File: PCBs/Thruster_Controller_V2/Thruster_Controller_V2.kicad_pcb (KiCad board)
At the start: 4 copper layers, 36 x 37.5 mm, 110 parts, among them J1 PHASE_A, J2 PHASE_B, J3 PHASE_C, J4 Conn_01x01, J5 Pogo Conn, J6 Conn_01x01, J7 Conn_01x01, J8 Conn_01x01, Q1 SIZF906DT, Q2 SIZF906DT, Q3 SIZF906DT, U1 DRV8305, U2 RTQ2569-50GQW, U3 MCP2515, U4 TPS62172DSGR, U5 TMS320F28027F, U8 MCP2562, Y1 20MHz

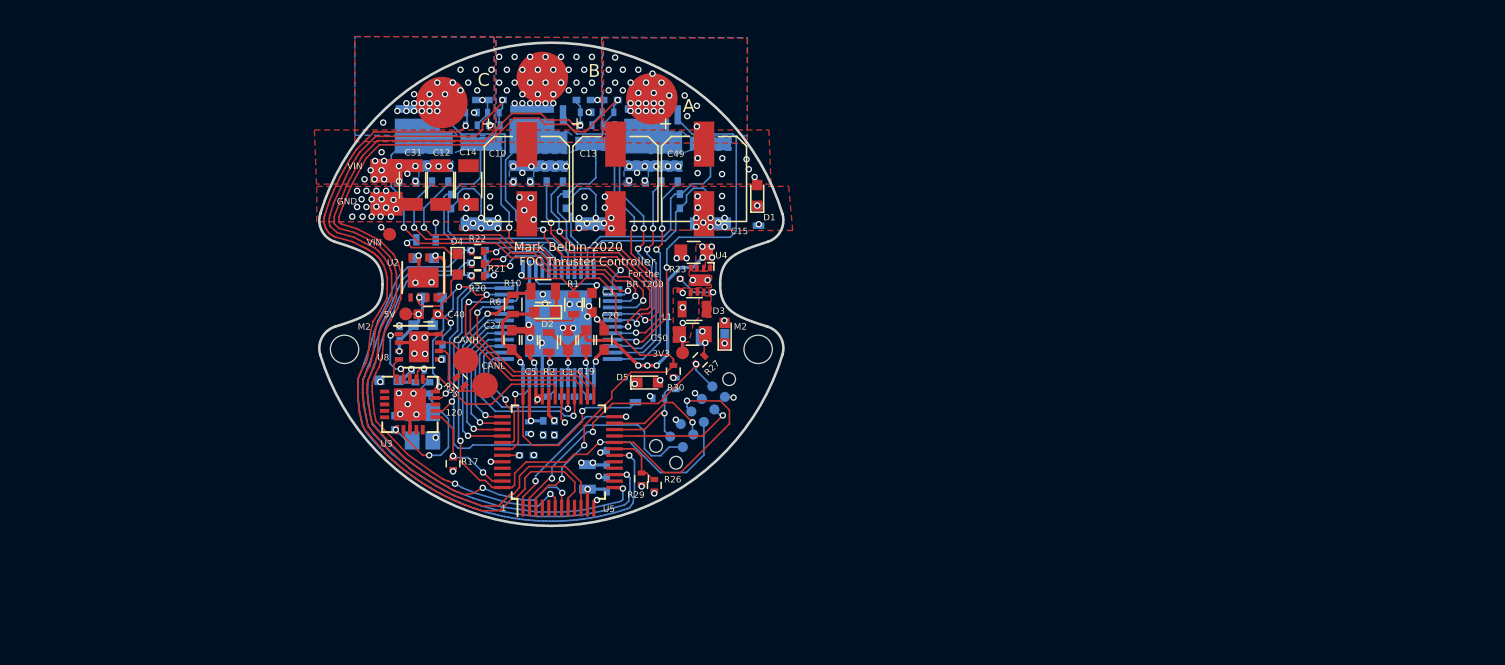
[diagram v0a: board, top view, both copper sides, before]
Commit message: Started Layout
- Imported new netlist
- Ripped up old tracks
- Added new outline
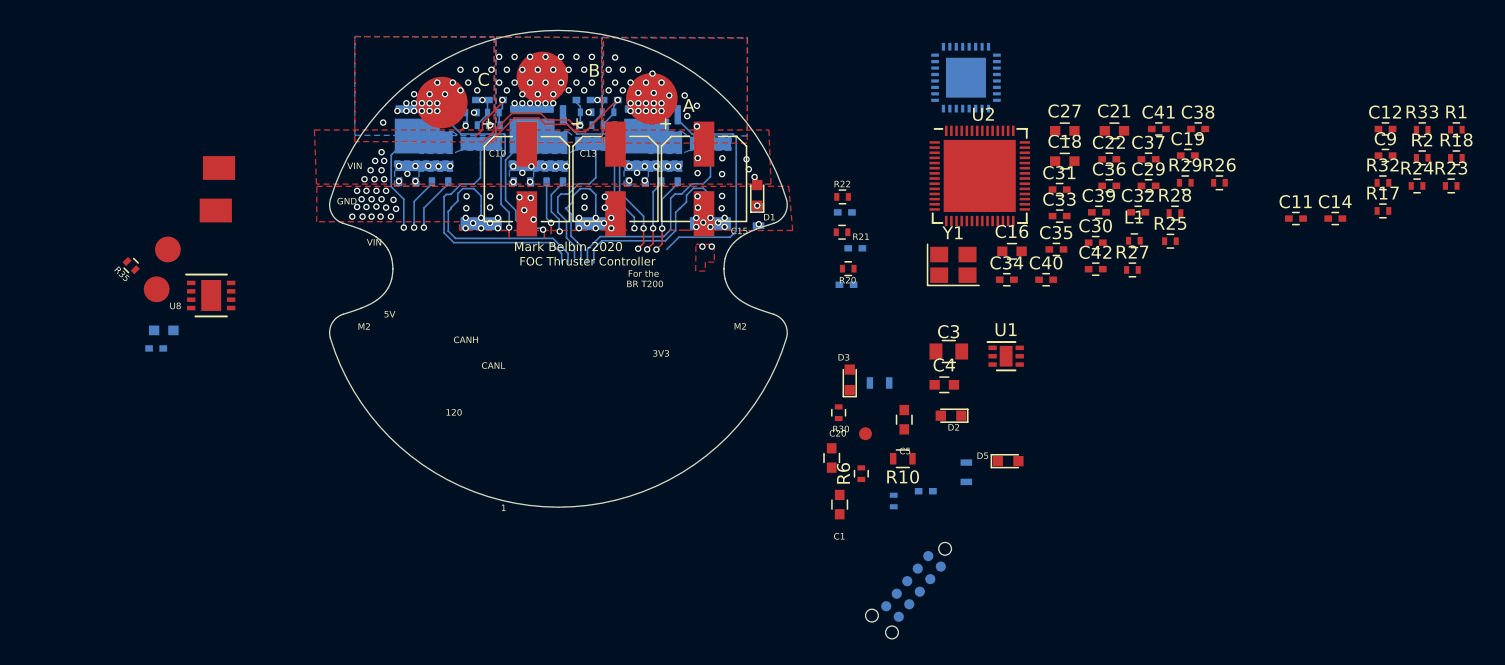
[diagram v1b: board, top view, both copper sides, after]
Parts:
- removed C49: 10uF, Capacitors_SMD:C_0805
- removed C50: 22uF, Capacitors_SMD:C_0805
- removed D4: RED, LEDs:LED_0603
- removed H1, H2: MountingHole, Thruster_Controller:MountingHole_M2
- removed L2: FB, Inductors_SMD:L_0805
- removed TP2, TP3: TestPoint, Thruster_Controller:TestPoint_Pad_D1.0mm
- removed U4: TPS62172DSGR, Thruster_Controller:8-Pin_WSON
- removed U5: TMS320F28027F, Housings_QFP:LQFP-48_7x7mm_Pitch0.5mm
- added C11: 0.01uF, Capacitors_SMD:C_0402, F.Cu at (157.2, 94.3)
- added C32: 2.2uF, Capacitors_SMD:C_0402, F.Cu at (145.0, 93.9)
- added C33: 0.1uF, Capacitors_SMD:C_0402, F.Cu at (138.9, 94.2)
- added R32: 2.49k, Resistors_SMD:R_0402, F.Cu at (164.0, 91.6)
- added R33: 56, Resistors_SMD:R_0402, F.Cu at (167.0, 87.5)
- C10, C13, C15: value 22uF -> 220uF
- C12, C14: value 22uF -> 0.01uF; footprint Capacitors_SMD:C_1206 -> Capacitors_SMD:C_0402
- C16, C18: value 1000pF -> 10uF; footprint Capacitors_SMD:C_0402 -> Capacitors_SMD:C_0603; moved to F.Cu
- C19: footprint Capacitors_SMD:C_0603 -> Capacitors_SMD:C_0402
- C21: value 15pF -> 10uF; footprint Capacitors_SMD:C_0402 -> Capacitors_SMD:C_0603; moved to F.Cu
- C22: value 15pF -> 2.2uF; moved to F.Cu
- C27: value 1uF -> 10uF
- C29: value 1uF -> 2.2uF; footprint Capacitors_SMD:C_0603 -> Capacitors_SMD:C_0402; moved to F.Cu
- C3: footprint Capacitors_SMD:C_0603 -> Capacitors_SMD:C_0805
- C30: value 0.1uF -> 2.2uF; moved to F.Cu
- C31: value 22uF -> 0.1uF; footprint Capacitors_SMD:C_1206 -> Capacitors_SMD:C_0402
- C34, C38: value 2.2uF -> 0.1uF; moved to F.Cu
- C35: value 2.2uF -> 10nF; moved to F.Cu
- C36, C37: value 2.2uF -> 9pF; moved to F.Cu
- C39, C41: value 1uF -> 0.1uF; footprint Capacitors_SMD:C_0603 -> Capacitors_SMD:C_0402; moved to F.Cu
- C4: value 0.047uF -> 1uF; footprint Capacitors_SMD:C_0402 -> Capacitors_SMD:C_0603; moved to F.Cu
- C40: value 1uF -> 0.1uF; footprint Capacitors_SMD:C_0603 -> Capacitors_SMD:C_0402
- C42: moved to F.Cu
- C9: value 1000pF -> 0.1uF; moved to F.Cu
- L1: value 2.2uH -> 220 Ohm; footprint Inductors_SMD:L_0805 -> Inductors_SMD:L_0402
- L3: value FB -> 60 Ohm
- R1: value 10k -> 2.2k; footprint Resistors_SMD:R_0603 -> Resistors_SMD:R_0402
- R10, R19: footprint Resistors_SMD:R_0805 -> Resistors_SMD:R_0603
- R17: value 10k -> 27.4k
- R18: value 10k -> 27.4k; moved to F.Cu
- R2: value 100 -> 27.4k; footprint Resistors_SMD:R_0603 -> Resistors_SMD:R_0402
- R23: value 100k -> 2.49k; footprint Resistors_SMD:R_0402_NoSilk -> Resistors_SMD:R_0402
- R24: value 680 -> 2.49k; footprint Resistors_SMD:R_0603 -> Resistors_SMD:R_0402; moved to F.Cu
- R25: value 820 -> 10k; moved to F.Cu
- R26: value 820 -> 10k
- R28: value 2.2k -> 10k; moved to F.Cu
- R29: value 2.2k -> 10k
- R6: footprint Resistors_SMD:R_0603 -> Resistors_SMD:R_0402
- U1: value DRV8305 -> NCP718AMT330; footprint Thruster_Controller:DRV8305 -> Housings_DFN_QFN:DFN-6-1EP_2x2mm_Pitch0.65mm; moved to F.Cu
- U2: value RTQ2569-50GQW -> TMS320F280041C; footprint Housings_DFN_QFN:DFN-8-1EP_3x3mm_Pitch0.65mm -> Housings_DFN_QFN:QFN-56-1EP_7x7mm_Pitch0.4mm
- U3: value MCP2515 -> DRV8320S; footprint Housings_DFN_QFN:QFN-20-1EP_4x4mm_Pitch0.5mm -> Housings_DFN_QFN:WQFN-32-1EP_5x5mm_Pitch0.5mm; moved to B.Cu
- Y1: value 20MHz -> 20 MHz; footprint Crystals:Crystal_SMD_SeikoEpson_TSX3225-4pin_3.2x2.5mm -> Crystals:Crystal_SMD_SeikoEpson_FA238-4pin_3.2x2.5mm; moved to F.Cu
- moved R18 82.2 mm to (169.7, 89.6)
- moved R24 77.0 mm to (166.6, 91.8)
- moved R17 74.8 mm to (164.0, 93.8), turned to 0 degrees
- moved C12 73.5 mm to (164.2, 87.4), turned to 0 degrees
- moved R1 69.8 mm to (169.7, 87.5), turned to 0 degrees
- moved R2 69.3 mm to (167.0, 89.6), turned to 0 degrees
- moved C14 67.3 mm to (160.3, 94.3), turned to 0 degrees
- moved R23 60.3 mm to (169.3, 91.8), turned to 0 degrees
- moved C21 60.3 mm to (143.1, 87.5), turned to 0 degrees
- moved C41 57.9 mm to (146.6, 87.4)
- moved C29 57.3 mm to (145.8, 91.8)
- moved C22 56.3 mm to (142.7, 89.7), turned to 0 degrees
- moved C38 55.1 mm to (149.6, 87.4), turned to 0 degrees
- moved C9 54.9 mm to (164.2, 89.5), turned to 0 degrees
- moved C30 54.5 mm to (141.7, 96.2), turned to 0 degrees
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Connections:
- net /TI_MCU/ADCINB7 renamed Net-(C26-Pad1)
- C12 pad 2: GND -> /Powertrain/SL_B
- C14 pad 2: GND -> /Powertrain/SL_C
- C16 pad 1: /Powertrain/SN2 -> +3V3
- C16 pad 2: /Powertrain/SP2 -> GND
- C17 pad 1: /TI_MCU/ADCINA0 -> /Powertrain/VSEN_C
- C18 pad 1: /Powertrain/SN3 -> +3V3
- C18 pad 2: /Powertrain/SP3 -> GND
- C19 pad 1: +BATT -> +3V3
- C19 pad 2: Net-(C19-Pad2) -> GND
- C21 pad 1: Net-(C21-Pad1) -> +3V3
- C24 pad 1: /TI_MCU/ADCINB1 -> Net-(C24-Pad1)
- C24 pad 2: GND -> /Powertrain/PGA_GND
- C25 pad 1: /TI_MCU/ADCINB3 -> Net-(C25-Pad1)
- C25 pad 2: GND -> /Powertrain/PGA_GND
- C26 pad 2: GND -> /Powertrain/PGA_GND
- C27 pad 1: +3V3 -> +3.3VA
- C29 pad 1: +5V -> Net-(C22-Pad1)
- C3 pad 1: Net-(C3-Pad1) -> +BATT
- C30 pad 1: +5V -> Net-(C30-Pad1)
- C31 pad 1: +BATT -> +3V3
- C34 pad 1: Net-(C34-Pad1) -> +3.3VA
- C35 pad 1: +3V3 -> /TI_MCU/~RESET~
- C36 pad 1: Net-(C36-Pad1) -> /TI_MCU/X1
- C37 pad 1: Net-(C37-Pad1) -> /TI_MCU/X2
- C38 pad 1: Net-(C38-Pad1) -> +3V3
- C39 pad 1: +BATT -> +3.3VA
- C4 pad 1: Net-(C4-Pad1) -> +3V3
- C4 pad 2: Net-(C4-Pad2) -> GND
- C40 pad 1: +5V -> +3.3VA
- C41 pad 1: +5V -> +3V3
- C42 pad 1: +3V3 -> +3.3VA
- C5 pad 1: Net-(C5-Pad1) -> +BATT
- C5 pad 2: GND -> Net-(C5-Pad2)
- C6 pad 1: /TI_MCU/ADCINA3 -> /Powertrain/VSEN_B
- C7 pad 1: /TI_MCU/ADCINA1 -> /Powertrain/VSEN_C
- C8 pad 1: /TI_MCU/ADCINA7 -> /Powertrain/VSEN_A
- C9 pad 1: /Powertrain/SN1 -> +BATT
- C9 pad 2: /Powertrain/SP1 -> GND
- J5 pad 3: /GPIO28 -> /SCI_TX
- J5 pad 5: /GPIO29 -> /SCI_RX
- L1 pad 1: Net-(L1-Pad1) -> +3V3
- L1 pad 2: +3V3 -> +3.3VA
- L3 pad 2: Net-(C37-Pad1) -> Net-(C22-Pad1)
- NT1 pad 1: /Powertrain/SP2 -> /Powertrain/SNA
- NT2 pad 1: /Powertrain/SP3 -> /Powertrain/SNA
- NT3 pad 1: /Powertrain/SP1 -> /Powertrain/SNA
- NT4 pad 1: /Powertrain/SN2 -> /Powertrain/SPB
- NT5 pad 1: /Powertrain/SN3 -> /Powertrain/SPC
- NT6 pad 1: /Powertrain/SN1 -> /Powertrain/SPA
- R1 pad 2: /Powertrain/PWRGD -> /Powertrain/SPI_MISO
- R10 pad 2: /GPIO28 -> /Powertrain/nFAULT
- R12 pad 1: /TI_MCU/ADCINA3 -> /Powertrain/VSEN_B
- R13 pad 1: /TI_MCU/ADCINA1 -> /Powertrain/VSEN_C
- R14 pad 1: /TI_MCU/ADCINA7 -> /Powertrain/VSEN_A
- R15 pad 2: /TI_MCU/ADCINA0 -> /Powertrain/VSEN_C
- R16 pad 1: /TI_MCU/ADCINA0 -> /Powertrain/VSEN_C
- R17 pad 1: +3V3 -> /Powertrain/ISEN_B
- R17 pad 2: /TI_MCU/CAN_INT -> /Powertrain/DAC
- R18 pad 1: +3V3 -> /Powertrain/ISEN_C
- R18 pad 2: Net-(R18-Pad2) -> /Powertrain/DAC
- R2 pad 1: +BATT -> /Powertrain/ISEN_A
- R2 pad 2: Net-(R2-Pad2) -> /Powertrain/DAC
- R20 pad 1: /Powertrain/ISEN_A_DRV -> /Powertrain/SPA
- R20 pad 2: /TI_MCU/ADCINB1 -> Net-(C24-Pad1)
- R21 pad 1: /Powertrain/ISEN_B_DRV -> /Powertrain/SPB
- R21 pad 2: /TI_MCU/ADCINB3 -> Net-(C25-Pad1)
- R22 pad 1: /Powertrain/ISEN_C_DRV -> /Powertrain/SPC
- R23 pad 1: +3V3 -> Net-(C24-Pad1)
- R23 pad 2: Net-(R23-Pad2) -> /Powertrain/ISEN_A
- R24 pad 1: Net-(D4-Pad1) -> Net-(C25-Pad1)
- R24 pad 2: GND -> /Powertrain/ISEN_B
- R25 pad 2: /TDO -> /TDI
- R26 pad 2: /TI_MCU/GPIO34 -> /TDO
- R27 pad 1: /TRST -> +3V3
- R27 pad 2: GND -> /TMS
- R28 pad 1: /TDO -> +3V3
- R28 pad 2: GND -> /TI_MCU/GPIO32
- R29 pad 1: /TI_MCU/GPIO34 -> +3V3
- R29 pad 2: GND -> /TI_MCU/GPIO24
- R3 pad 2: /TI_MCU/ADCINA3 -> /Powertrain/VSEN_B
- R30 pad 2: /Powertrain/PWRGD -> /TI_MCU/~RESET~
- R31 pad 2: /TI_MCU/GPIO33 -> /TI_MCU/GPIO6
- R4 pad 2: /TI_MCU/ADCINA1 -> /Powertrain/VSEN_C
- R5 pad 2: /TI_MCU/ADCINA7 -> /Powertrain/VSEN_A
- R6 pad 2: /GPIO28 -> /Powertrain/nFAULT
- U1 pad 1: /Powertrain/EN_GATE -> +3V3
- U1 pad 2: /TI_MCU/EPWM1A -> GND
- U1 pad 3: /TI_MCU/EPWM1B -> GND
- U1 pad 4: /TI_MCU/EPWM2A -> +BATT
- U1 pad 5: /TI_MCU/EPWM2B -> GND
- U1 pad 6: /TI_MCU/EPWM3A -> +BATT
- U1 pad 7: /TI_MCU/EPWM3B -> GND
- U2 pad 1: +BATT -> /TI_MCU/GPIO6
- U2 pad 2: Net-(U2-Pad2) -> /SCI_TX
- U2 pad 3: GND -> /SCI_RX
- U2 pad 4: Net-(U2-Pad4) -> /TI_MCU/~RESET~
- U2 pad 5: Net-(U2-Pad5) -> +3V3
- U2 pad 6: +5V -> /Powertrain/VSEN_C
- U2 pad 7: Net-(U2-Pad7) -> /Powertrain/VSEN_B
- U2 pad 8: +BATT -> /Powertrain/VSEN_A
- U2 pad 9: GND -> /Powertrain/PGA_GND
- U3 pad 1: Net-(U3-Pad1) -> Net-(C2-Pad2)
- U3 pad 10: Net-(U3-Pad10) -> /Powertrain/GL_B
- U3 pad 11: /TI_MCU/CAN_INT -> /Powertrain/SH_B
- U3 pad 12: /Powertrain/SPI_CLK -> /Powertrain/GH_B
- U3 pad 13: Net-(U3-Pad13) -> /Powertrain/GH_C
- U3 pad 14: /Powertrain/SPI_MOSI -> /Powertrain/SH_C
- U3 pad 15: /Powertrain/SPI_MISO -> /Powertrain/GL_C
- U3 pad 16: /TI_MCU/SPI_CS_1 -> /Powertrain/SL_C
- U3 pad 17: Net-(R18-Pad2) -> /Powertrain/nFAULT
- U3 pad 18: +3V3 -> /Powertrain/SPI_MISO
- U3 pad 19: /TXCAN -> /Powertrain/SPI_MOSI
- U3 pad 2: Net-(U3-Pad2) -> Net-(C5-Pad2)
- U3 pad 20: /RXCAN -> /Powertrain/SPI_CLK
- U3 pad 21: GND -> /Powertrain/SPI_CS
- U3 pad 3: Net-(U3-Pad3) -> +BATT
- U3 pad 4: Net-(U3-Pad4) -> +BATT
- U3 pad 5: Net-(U3-Pad5) -> /Powertrain/GH_A
- U3 pad 6: Net-(C21-Pad1) -> /Powertrain/SH_A
- U3 pad 7: Net-(C22-Pad1) -> /Powertrain/GL_A
- U3 pad 8: GND -> /Powertrain/SL_A
- U3 pad 9: Net-(U3-Pad9) -> /Powertrain/SL_B
- U8 pad 3: +5V -> +3V3
- Y1 pad 1: Net-(C22-Pad1) -> /TI_MCU/X1
- Y1 pad 3: Net-(C21-Pad1) -> /TI_MCU/X2
- Y1 pad 4: GND -> (no net)
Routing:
- net /TI_MCU/ADCINA7: track 65.9 -> 0.00 mm, vias 3 -> 0
- net /TI_MCU/ADCINA3: track 64.1 -> 0.00 mm, vias 3 -> 0
- net /TI_MCU/ADCINA0: track 63.3 -> 0.00 mm, vias 1 -> 0
- net /TI_MCU/ADCINA1: track 59.6 -> 0.00 mm, vias 1 -> 0
- net GND: track 64.1 -> 10.4 mm, vias 111 -> 61
- net Net-(C26-Pad1): track 47.5 -> 0.00 mm, vias 2 -> 0
- net /GPIO28: track 44.4 -> 0.00 mm, vias 3 -> 0
- net /TI_MCU/ADCINB3: track 43.9 -> 0.00 mm, vias 2 -> 0
- net /Powertrain/SNA: track 0.00 -> 40.3 mm
- net /TI_MCU/ADCINB1: track 40.2 -> 0.00 mm, vias 2 -> 0
- net /Powertrain/PWRGD: track 35.7 -> 0.00 mm, vias 3 -> 0
- net /Powertrain/SPI_MOSI: track 33.0 -> 0.00 mm, vias 2 -> 0
- net /Powertrain/SPI_CLK: track 32.3 -> 0.00 mm, vias 2 -> 0
- net +BATT: track 34.2 -> 3.34 mm, vias 51 -> 43
- net /Powertrain/SPI_MISO: track 28.3 -> 0.00 mm, vias 3 -> 0
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- removed copper zone on F.Cu, net +3V3
- removed copper zone on F.Cu, net Net-(L1-Pad1)
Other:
- board size 36 x 37.5 mm -> 35.5 x 37 mm
- board text added: "For Instructional Use Only."
- board text added: "SOLIDWORKS Educational Product."

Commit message: Restart
- Semester is over, back to work
- Starting by ripping up all tracks
- Component placement for powertrain, still need to look at feedback signals
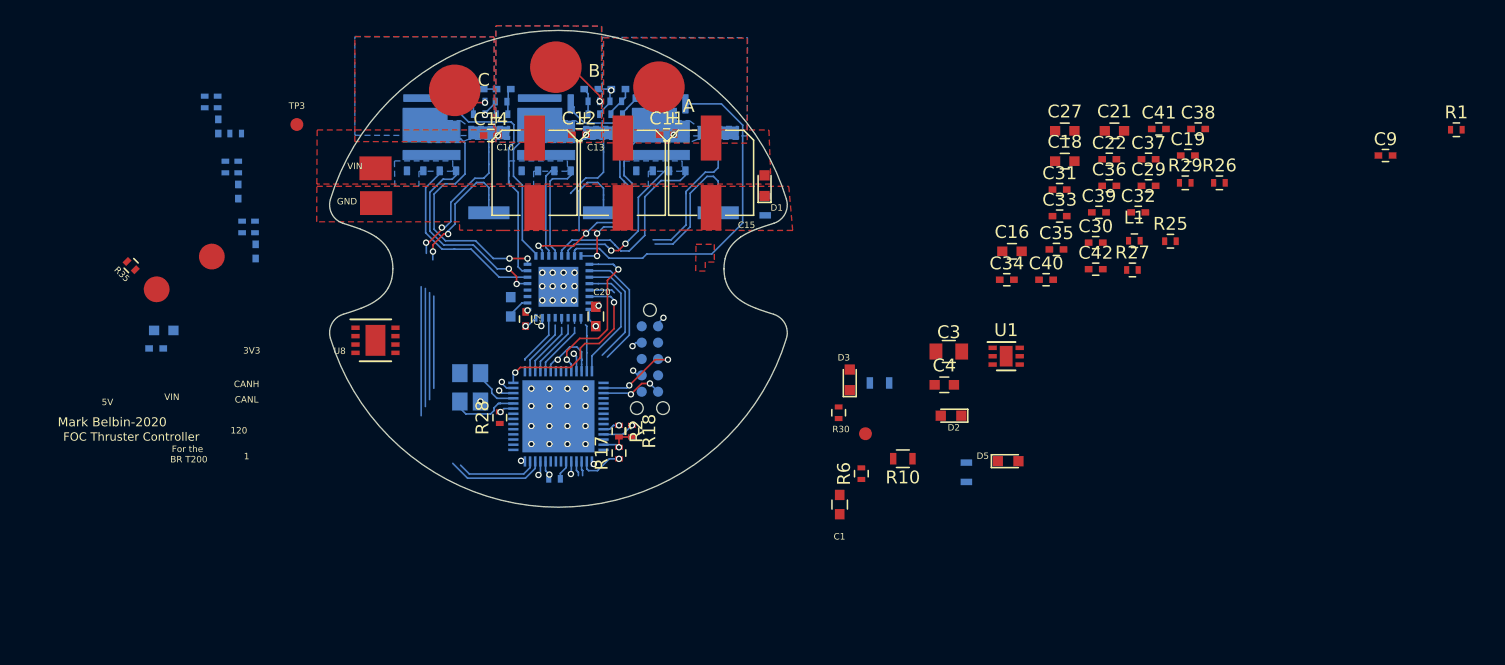
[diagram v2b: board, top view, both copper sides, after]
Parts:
- added TP3: TestPoint, Thruster_Controller:TestPoint_Pad_D1.0mm, F.Cu at (79.7, 87.0)
- C2: moved to F.Cu
- C5, R20, R21, R22, R23, R24, R32, R33, U2, Y1: moved to B.Cu
- moved R23 97.0 mm to (72.5, 85.3), turned to 270 degrees
- moved R24 92.5 mm to (74.2, 90.3), turned to 270 degrees
- moved R33 92.1 mm to (75.0, 87.8)
- moved R32 88.6 mm to (75.5, 95.0), turned to 270 degrees
- moved R18 67.4 mm to (105.7, 110.8), turned to 270 degrees
- moved C14 65.9 mm to (94.8, 87.9)
- moved R2 65.8 mm to (104.7, 110.8), turned to 270 degrees
- moved C12 62.6 mm to (101.6, 87.8)
- moved R17 62.2 mm to (104.7, 112.5), turned to 90 degrees
- moved R28 54.8 mm to (95.5, 109.8), turned to 90 degrees
- moved R20 50.6 mm to (73.5, 85.3), turned to 270 degrees
- moved C24 50.3 mm to (73.6, 87.2), turned to 270 degrees
- moved C11 49.3 mm to (108.4, 87.8)
- moved C25 48.1 mm to (75.2, 92.2), turned to 270 degrees
- moved R21 47.1 mm to (75.2, 90.3), turned to 270 degrees
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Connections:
- C11 pad 2: /Powertrain/SL_A -> /Powertrain/SL_C
- C14 pad 2: /Powertrain/SL_C -> /Powertrain/SL_A
- C7 pad 1: /Powertrain/VSEN_C -> /Powertrain/VSEN_A
- C8 pad 1: /Powertrain/VSEN_A -> /Powertrain/VSEN_C
- NT5 pad 1: /Powertrain/SPC -> /Powertrain/SPA
- NT5 pad 2: /Powertrain/SL_C -> /Powertrain/SL_A
- NT6 pad 1: /Powertrain/SPA -> /Powertrain/SPC
- NT6 pad 2: /Powertrain/SL_A -> /Powertrain/SL_C
- Q2 pad 1: /Powertrain/GH_C -> /Powertrain/GH_A
- Q2 pad 2: /Powertrain/SH_C -> /Powertrain/SH_A
- Q2 pad 3: /Powertrain/GL_C -> /Powertrain/GL_A
- Q2 pad 5: /Powertrain/Phase_C -> /Powertrain/Phase_A
- Q2 pad 6: /Powertrain/SL_C -> /Powertrain/SL_A
- Q3 pad 1: /Powertrain/GH_A -> /Powertrain/GH_C
- Q3 pad 2: /Powertrain/SH_A -> /Powertrain/SH_C
- Q3 pad 3: /Powertrain/GL_A -> /Powertrain/GL_C
- Q3 pad 5: /Powertrain/Phase_A -> /Powertrain/Phase_C
- Q3 pad 6: /Powertrain/SL_A -> /Powertrain/SL_C
- R11 pad 1: /Powertrain/SL_A -> /Powertrain/SL_C
- R13 pad 1: /Powertrain/VSEN_C -> /Powertrain/VSEN_A
- R14 pad 1: /Powertrain/VSEN_A -> /Powertrain/VSEN_C
- R4 pad 1: /Powertrain/Phase_C -> /Powertrain/Phase_A
- R4 pad 2: /Powertrain/VSEN_C -> /Powertrain/VSEN_A
- R5 pad 1: /Powertrain/Phase_A -> /Powertrain/Phase_C
- R5 pad 2: /Powertrain/VSEN_A -> /Powertrain/VSEN_C
- R9 pad 1: /Powertrain/SL_C -> /Powertrain/SL_A
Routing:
- net /Powertrain/SNA: track 40.3 -> 25.1 mm, vias 0 -> 2
- net /Powertrain/EN_GATE: track 0.00 -> 14.6 mm, vias 0 -> 2
- net /Powertrain/ISEN_B: track 0.00 -> 13.5 mm, vias 0 -> 1
- net /Powertrain/GL_C: track 14.2 -> 27.7 mm, vias 1 -> 0
- net /Powertrain/nFAULT: track 0.00 -> 13.0 mm, vias 0 -> 2
- net /Powertrain/VSEN_A: track 14.9 -> 2.07 mm, vias 1 -> 0
- net /Powertrain/ISEN_C: track 0.00 -> 11.7 mm, vias 0 -> 1
- net /Powertrain/GH_C: track 4.40 -> 15.3 mm, vias 1 -> 0
- net /Powertrain/SL_A: track 12.1 -> 22.7 mm, vias 2 -> 3
- net /Powertrain/SPI_CLK: track 0.00 -> 9.74 mm
- net /Powertrain/SPI_MISO: track 0.00 -> 9.64 mm
- net /Powertrain/ISEN_A: track 0.00 -> 9.62 mm, vias 0 -> 1
- net /Powertrain/GH_A: track 6.00 -> 15.6 mm
- net /Powertrain/SPI_MOSI: track 0.00 -> 8.91 mm
- net /Powertrain/SH_A: track 5.77 -> 14.6 mm, vias 2 -> 0
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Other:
- board text removed: "For Instructional Use Only."
- board text removed: "M2"
- board text removed: "SOLIDWORKS Educational Product."

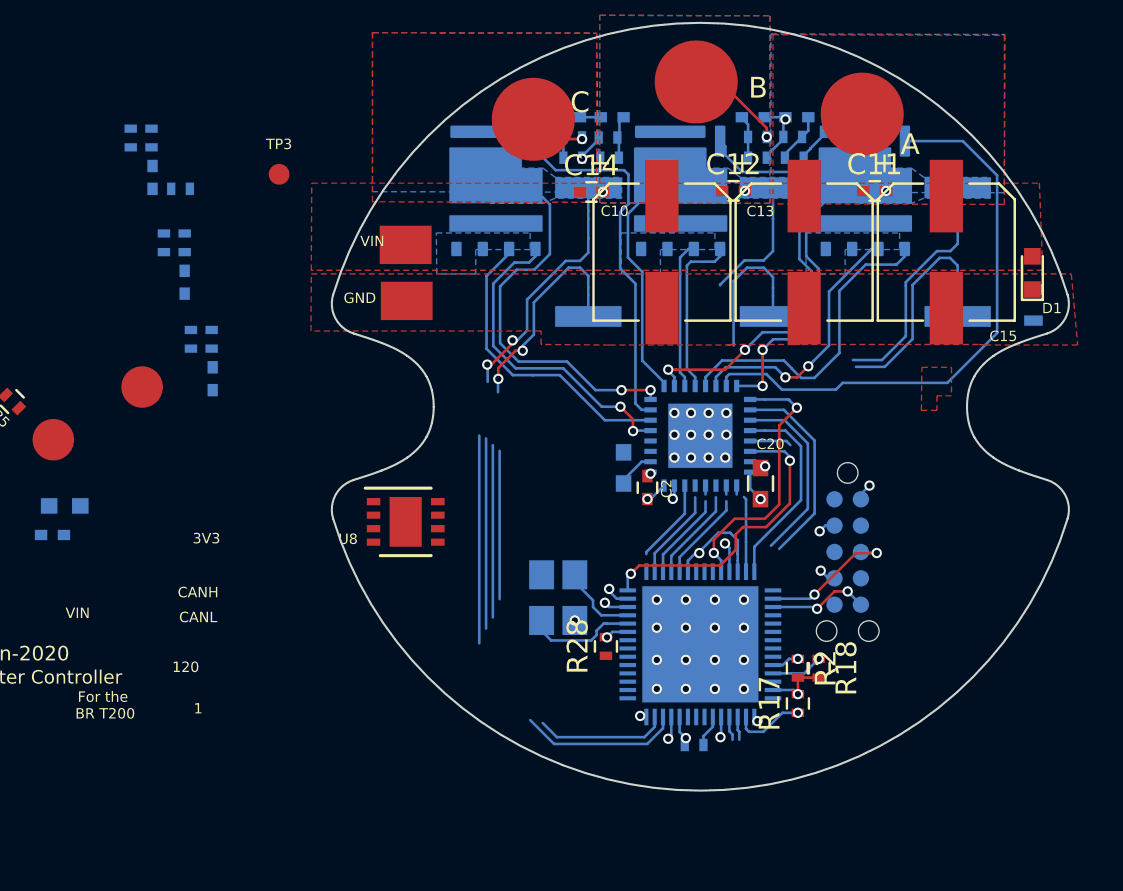
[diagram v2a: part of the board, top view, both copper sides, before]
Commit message: More Routing
- Routed ISEN lines better
- Need to figure out VSEN
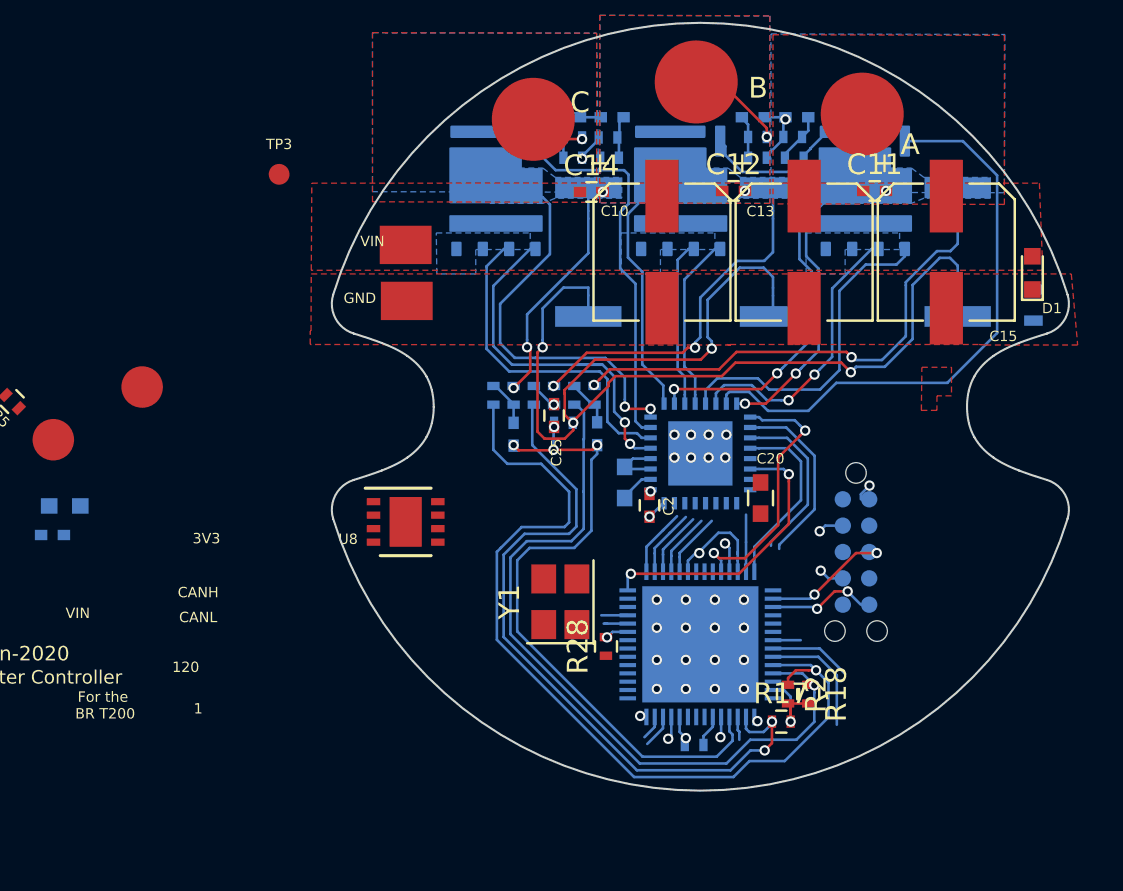
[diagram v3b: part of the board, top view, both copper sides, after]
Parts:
- C25, Y1: moved to F.Cu
- moved R33 21.6 mm to (93.4, 99.0), turned to 180 degrees
- moved R23 21.4 mm to (90.0, 97.7)
- moved R20 21.4 mm to (91.0, 97.7)
- moved C24 21.4 mm to (91.0, 99.6)
- moved R24 19.3 mm to (92.0, 97.7)
- moved R21 19.3 mm to (93.0, 97.7)
- moved C25 18.9 mm to (93.0, 98.7)
- moved C26 18.7 mm to (95.0, 99.5)
- moved R32 18.7 mm to (93.9, 97.7)
- moved R22 18.6 mm to (94.9, 97.7)
- moved R18 1.35 mm to (105.2, 112.1)
- moved R2 1.34 mm to (104.2, 112.1)
- moved R17 1.19 mm to (103.9, 113.4), turned to 0 degrees
- moved C2 0.86 mm to (97.5, 103.0)
- moved U3 0.85 mm to (100.0, 100.5)
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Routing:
- net /Powertrain/ISEN_A: track 9.62 -> 42.9 mm
- net /Powertrain/PGA_GND: track 8.31 -> 37.6 mm, vias 0 -> 4
- net /Powertrain/SNA: track 25.1 -> 52.8 mm, vias 2 -> 4
- net /Powertrain/ISEN_C: track 11.7 -> 36.5 mm
- net /Powertrain/ISEN_B: track 13.5 -> 34.1 mm, vias 1 -> 2
- net /Powertrain/SPC: track 10.1 -> 23.4 mm, vias 0 -> 2
- net /Powertrain/SPB: track 4.81 -> 16.3 mm, vias 0 -> 2
- net /RXCAN: track 7.73 -> 1.61 mm
- net /TXCAN: track 6.36 -> 1.18 mm
- net /Powertrain/INL_C: track 7.71 -> 2.75 mm
- net /TI_MCU/X2: track 5.40 -> 1.26 mm
- net /Powertrain/VSEN_A: track 2.07 -> 6.06 mm
- net /Powertrain/INH_C: track 0.00 -> 3.29 mm
- net +BATT: track 0.00 -> 2.71 mm
- net /Powertrain/GH_A: track 15.6 -> 18.0 mm
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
